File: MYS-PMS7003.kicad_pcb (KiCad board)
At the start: 2 copper layers, 92 x 60 mm, 42 parts, among them P1 CONN_02X04, P2 CONN_01X03, P3 CONN_01X08, P4 CONN_01X04, P5 CONN_01X04, P6 CONN_02X11, P7 CONN_01X06, U1 Arduino_Pro_Micro, U2 M3_Mounting_hole, U3 M3_Mounting_hole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

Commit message: Added text to silkscreen, added Gerber files, schematic.
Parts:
- added G***: LOGO, Open_Hardware:Full_OSHW_scaled, F.Cu at (89.0, 59.5)
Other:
- board text added: "MYS-PMS7003 Rev.0"
- board text added: "https://github.com/dirkjankrijnders/MYS-PMS7003"

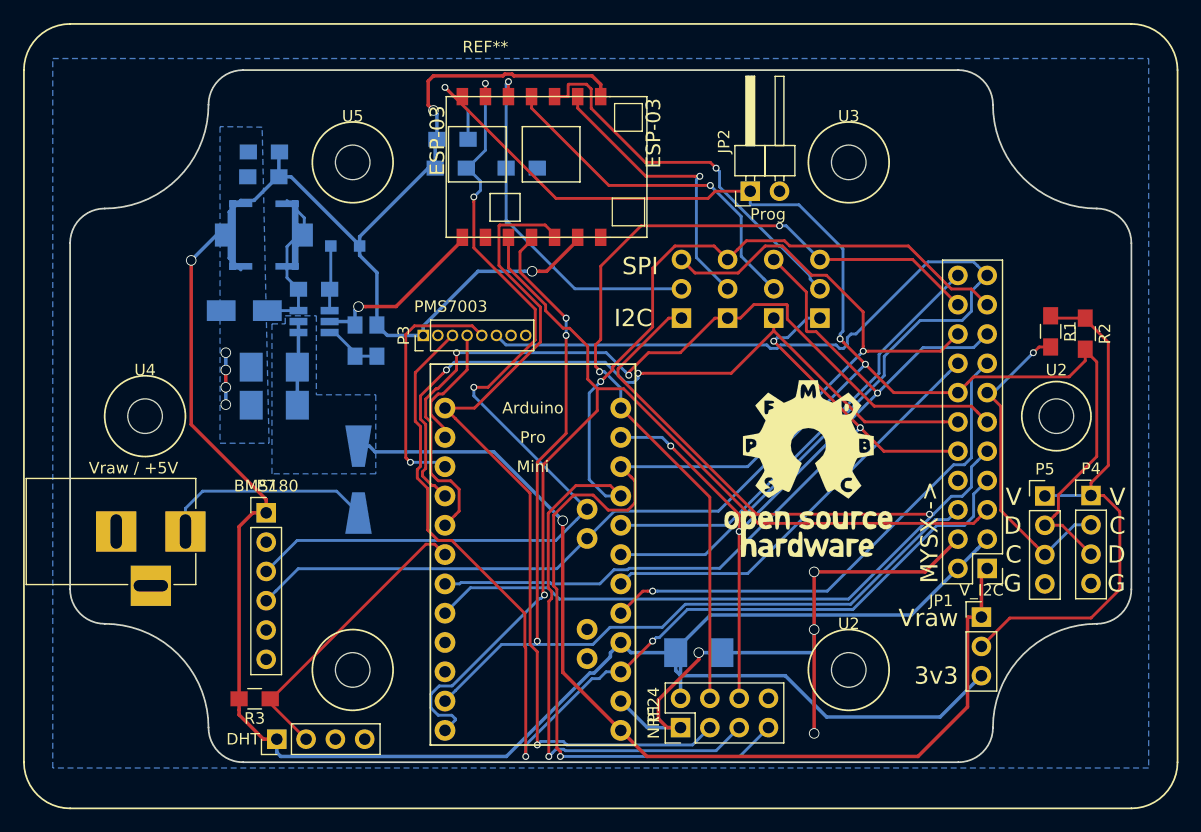
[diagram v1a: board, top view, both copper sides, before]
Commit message: Updated radio module outline, fixed missing tracks
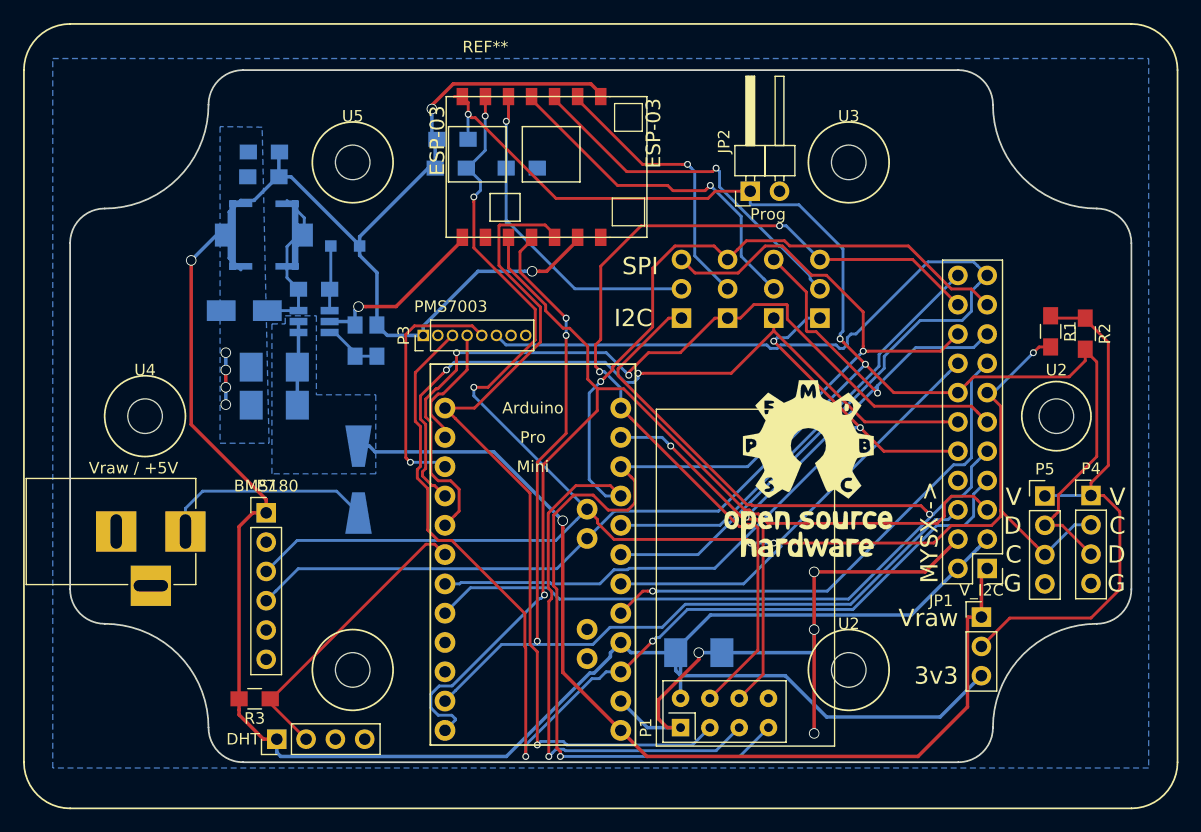
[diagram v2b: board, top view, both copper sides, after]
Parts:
- P1: footprint Pin_Headers:Pin_Header_Straight_2x04_Pitch2.54mm -> RF_Modules:nRF24L01_Breakout
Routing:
- net /MYSX_D7_SCL: track 107.1 -> 143.5 mm, vias 4 -> 6
- net /MYSX_D8_SDA: track 164.9 -> 159.3 mm
- net /MYSX_D14_CS: track 77.4 -> 81.9 mm
- net +3V3: track 245.1 -> 242.2 mm
- net Net-(JP4-Pad2): track 31.4 -> 28.8 mm
- net Net-(JP3-Pad2): track 33.3 -> 31.2 mm
- net /MYSX_D11_MOSI: track 73.3 -> 75.2 mm
- net /MYSX_D1_DFM: track 94.1 -> 95.8 mm
- net Net-(JP5-Pad2): track 25.0 -> 24.3 mm

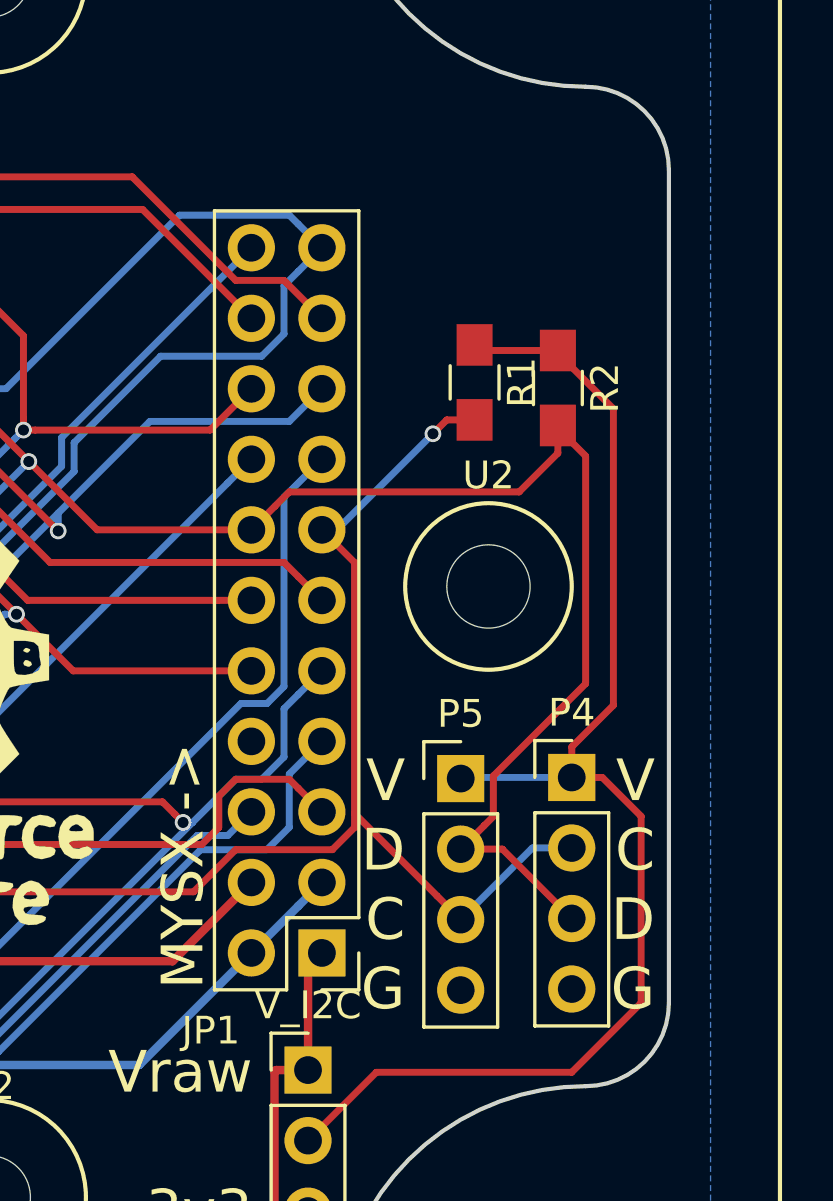
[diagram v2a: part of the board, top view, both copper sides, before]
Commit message: Created a slot for the MYSX cable to go to the other side of the board
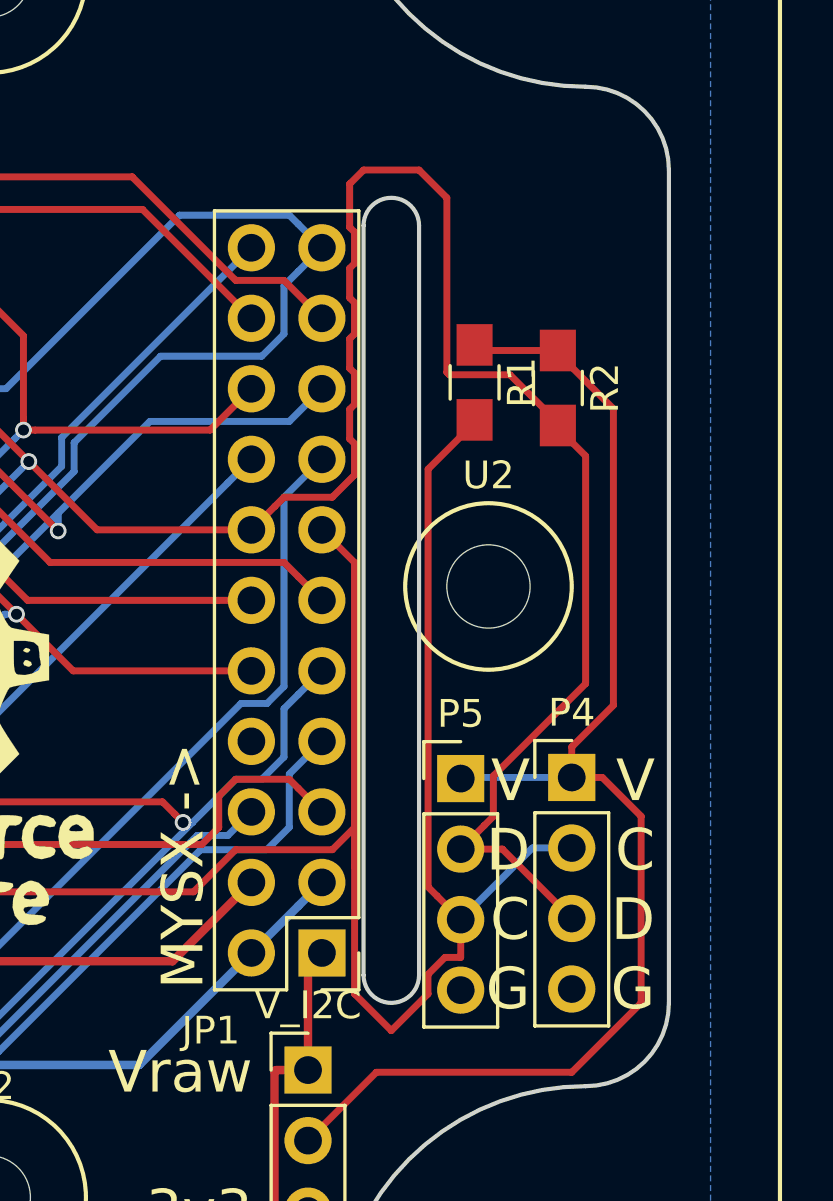
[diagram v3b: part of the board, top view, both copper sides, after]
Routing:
- net /MYSX_D7_SCL: track 143.5 -> 163.9 mm, vias 6 -> 5
- net /MYSX_D8_SDA: track 159.3 -> 176.9 mm
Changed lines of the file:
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@@
     (area 20.721799 20.721799 121.278201 89.278201)
     (thickness 1.6)
-    (drawings 15)
-    (tracks 702)
+    (drawings 19)
+    (tracks 731)
     (zones 0)
     (modules 43)
@@
       (net 22 "Net-(P1-Pad8)"))
   )
+  (gr_line (start 108 69) (end 108 42) (layer Edge.Cuts) (width 0.15))
+  (gr_line (start 106 42) (end 106 69) (layer Edge.Cuts) (width 0.15))
+  (gr_arc (start 107 42) (end 106 42) (angle 180) (layer Edge.Cuts) (width 0.15))
+  (gr_arc (start 107 69) (end 108 69) (angle 180) (layer Edge.Cuts) (width 0.15))
   (gr_text https://github.com/dirkjankrijnders/MYS-PMS7003 (at 62.5 37) (layer B.SilkS)
     (effects (font (size 0.75 0.75) (thickness 0.15)) (justify mirror))
@@
     (effects (font (size 1.5 1.5) (thickness 0.3)) (justify right))
   )
-  (gr_text G (at 107.5 69.5) (layer F.SilkS)
+  (gr_text G (at 112 69.5) (layer F.SilkS)
     (effects (font (size 1.5 1.5) (thickness 0.3)) (justify right))
   )
-  (gr_text C (at 107.5 67) (layer F.SilkS)
+  (gr_text C (at 112 67) (layer F.SilkS)
     (effects (font (size 1.5 1.5) (thickness 0.3)) (justify right))
   )
-  (gr_text D (at 107.5 64.5) (layer F.SilkS)
+  (gr_text D (at 112 64.5) (layer F.SilkS)
     (effects (font (size 1.5 1.5) (thickness 0.3)) (justify right))
   )
-  (gr_text V (at 107.5 62) (layer F.SilkS)
+  (gr_text V (at 112 62) (layer F.SilkS)
     (effects (font (size 1.5 1.5) (thickness 0.3)) (justify right))
   )
@@
   (segment (start 113.5 61.88) (end 109.54 61.88) (width 0.25) (layer B.Cu) (net 7))
   (segment (start 109.54 61.88) (end 109.5 61.92) (width 0.25) (layer B.Cu) (net 7))
+  (segment (start 113 49.2) (end 113 49.1) (width 0.25) (layer F.Cu) (net 8))
+  (segment (start 109.089999 47.375001) (end 109 47.285002) (width 0.25) (layer F.Cu) (net 8))
+  (segment (start 111.275001 47.375001) (end 109.089999 47.375001) (width 0.25) (layer F.Cu) (net 8))
+  (segment (start 113 49.1) (end 111.275001 47.375001) (width 0.25) (layer F.Cu) (net 8))
+  (segment (start 109 41) (end 108 40) (width 0.25) (layer F.Cu) (net 8))
+  (segment (start 109 47.285002) (end 109 41) (width 0.25) (layer F.Cu) (net 8))
+  (segment (start 105.675001 44.775999) (end 105.675001 45.904001) (width 0.25) (layer F.Cu) (net 8))
+  (segment (start 105.5 44.600998) (end 105.675001 44.775999) (width 0.25) (layer F.Cu) (net 8))
+  (segment (start 105.5 43.539002) (end 105.5 44.600998) (width 0.25) (layer F.Cu) (net 8))
+  (segment (start 105.675001 43.364001) (end 105.5 43.539002) (width 0.25) (layer F.Cu) (net 8))
+  (segment (start 105.675001 42.235999) (end 105.675001 43.364001) (width 0.25) (layer F.Cu) (net 8))
+  (segment (start 108 40) (end 106 40) (width 0.25) (layer F.Cu) (net 8))
+  (segment (start 105.5 42.060998) (end 105.675001 42.235999) (width 0.25) (layer F.Cu) (net 8))
+  (segment (start 105.5 40.5) (end 105.5 42.060998) (width 0.25) (layer F.Cu) (net 8))
+  (segment (start 106 40) (end 105.5 40.5) (width 0.25) (layer F.Cu) (net 8))
+  (segment (start 105.675001 45.904001) (end 105.5 46.079002) (width 0.25) (layer F.Cu) (net 8))
+  (segment (start 105.5 46.079002) (end 105.5 47.140998) (width 0.25) (layer F.Cu) (net 8))
+  (segment (start 105.5 47.140998) (end 105.675001 47.315999) (width 0.25) (layer F.Cu) (net 8))
+  (segment (start 105.675001 47.315999) (end 105.675001 48.444001) (width 0.25) (layer F.Cu) (net 8))
+  (segment (start 105.675001 48.444001) (end 105.5 48.619002) (width 0.25) (layer F.Cu) (net 8))
+  (segment (start 105.5 48.619002) (end 105.5 49.680998) (width 0.25) (layer F.Cu) (net 8))
+  (segment (start 105.5 49.680998) (end 105.675001 49.855999) (width 0.25) (layer F.Cu) (net 8))
+  (segment (start 105.675001 49.855999) (end 105.675001 50.984001) (width 0.25) (layer F.Cu) (net 8))
+  (segment (start 105.675001 50.984001) (end 104.874003 51.784999) (width 0.25) (layer F.Cu) (net 8))
+  (segment (start 104.874003 51.784999) (end 103.135001 51.784999) (width 0.25) (layer F.Cu) (net 8))
+  (segment (start 103.135001 51.784999) (end 102.809999 52.110001) (width 0.25) (layer F.Cu) (net 8))
+  (segment (start 102.809999 52.110001) (end 101.96 52.96) (width 0.25) (layer F.Cu) (net 8))
   (segment (start 59.5122 28.829) (end 59.812199 29.128999) (width 0.25) (layer F.Cu) (net 8))
   (segment (start 59.812199 29.128999) (end 60.128999 29.128999) (width 0.25) (layer F.Cu) (net 8))
@@
   (segment (start 44.774999 68.225001) (end 42.849999 70.150001) (width 0.25) (layer B.Cu) (net 8))
   (segment (start 42.849999 70.150001) (end 42 71) (width 0.25) (layer B.Cu) (net 8))
-  (segment (start 113 49.2) (end 113 50.2) (width 0.25) (layer F.Cu) (net 8))
-  (segment (start 113 50.2) (end 111.604999 51.595001) (width 0.25) (layer F.Cu) (net 8))
-  (segment (start 111.604999 51.595001) (end 103.324999 51.595001) (width 0.25) (layer F.Cu) (net 8))
-  (segment (start 103.324999 51.595001) (end 102.809999 52.110001) (width 0.25) (layer F.Cu) (net 8))
-  (segment (start 102.809999 52.110001) (end 101.96 52.96) (width 0.25) (layer F.Cu) (net 8))
   (segment (start 109.5 64.46) (end 111 64.46) (width 0.25) (layer F.Cu) (net 8))
   (segment (start 111 64.46) (end 113.5 66.96) (width 0.25) (layer F.Cu) (net 8))
@@
   (segment (start 92.374998 48.199998) (end 92.699998 47.874998) (width 0.25) (layer B.Cu) (net 28))
   (segment (start 86.300001 49.125001) (end 86.600001 48.825001) (width 0.25) (layer B.Cu) (net 28))
+  (segment (start 110 49) (end 110 49.1) (width 0.25) (layer F.Cu) (net 31))
+  (segment (start 110 49.1) (end 108.324999 50.775001) (width 0.25) (layer F.Cu) (net 31))
+  (segment (start 108.324999 50.775001) (end 108.324999 65.824999) (width 0.25) (layer F.Cu) (net 31))
+  (segment (start 108.324999 65.824999) (end 108.650001 66.150001) (width 0.25) (layer F.Cu) (net 31))
+  (segment (start 108.650001 66.150001) (end 109.5 67) (width 0.25) (layer F.Cu) (net 31))
+  (segment (start 105.675001 63.175001) (end 105.675001 65.091263) (width 0.25) (layer F.Cu) (net 31))
+  (segment (start 105.678201 65.094463) (end 105.678201 69.678201) (width 0.25) (layer F.Cu) (net 31))
+  (segment (start 105.675001 65.091263) (end 105.678201 65.094463) (width 0.25) (layer F.Cu) (net 31))
+  (segment (start 105.678201 69.678201) (end 107 71) (width 0.25) (layer F.Cu) (net 31))
+  (segment (start 107 71) (end 108.321799 69.678201) (width 0.25) (layer F.Cu) (net 31))
+  (segment (start 108.321799 69.678201) (end 108.321799 68.974463) (width 0.25) (layer F.Cu) (net 31))
+  (segment (start 108.321799 68.974463) (end 108.934463 68.361799) (width 0.25) (layer F.Cu) (net 31))
+  (segment (start 108.934463 68.361799) (end 109.5 68.361799) (width 0.25) (layer F.Cu) (net 31))
+  (segment (start 109.5 68.361799) (end 109.5 67) (width 0.25) (layer F.Cu) (net 31))
   (segment (start 86 66) (end 99.876262 66) (width 0.25) (layer F.Cu) (net 31))
   (segment (start 99.876262 66) (end 101.394463 64.481799) (width 0.25) (layer F.Cu) (net 31))
@@
   (segment (start 67.107001 65.774999) (end 68.919001 63.962999) (width 0.25) (layer B.Cu) (net 31))
   (segment (start 42 68.46) (end 44.685001 65.774999) (width 0.25) (layer B.Cu) (net 31))
-  (segment (start 108.5 49.5) (end 105.04 52.96) (width 0.25) (layer B.Cu) (net 31))
-  (segment (start 105.04 52.96) (end 104.5 52.96) (width 0.25) (layer B.Cu) (net 31))
-  (segment (start 110 49) (end 109 49) (width 0.25) (layer F.Cu) (net 31))
-  (segment (start 109 49) (end 108.5 49.5) (width 0.25) (layer F.Cu) (net 31))
-  (via (at 108.5 49.5) (size 0.6) (drill 0.4) (layers F.Cu B.Cu) (net 31))
   (segment (start 104.5 52.96) (end 105.675001 54.135001) (width 0.25) (layer F.Cu) (net 31))
   (segment (start 105.675001 54.135001) (end 105.675001 63.175001) (width 0.25) (layer F.Cu) (net 31))
-  (segment (start 105.675001 63.175001) (end 108.650001 66.150001) (width 0.25) (layer F.Cu) (net 31))
-  (segment (start 108.650001 66.150001) (end 109.5 67) (width 0.25) (layer F.Cu) (net 31))
   (segment (start 113.5 64.42) (end 112.08 64.42) (width 0.25) (layer B.Cu) (net 31))
   (segment (start 112.08 64.42) (end 109.5 67) (width 0.25) (layer B.Cu) (net 31))

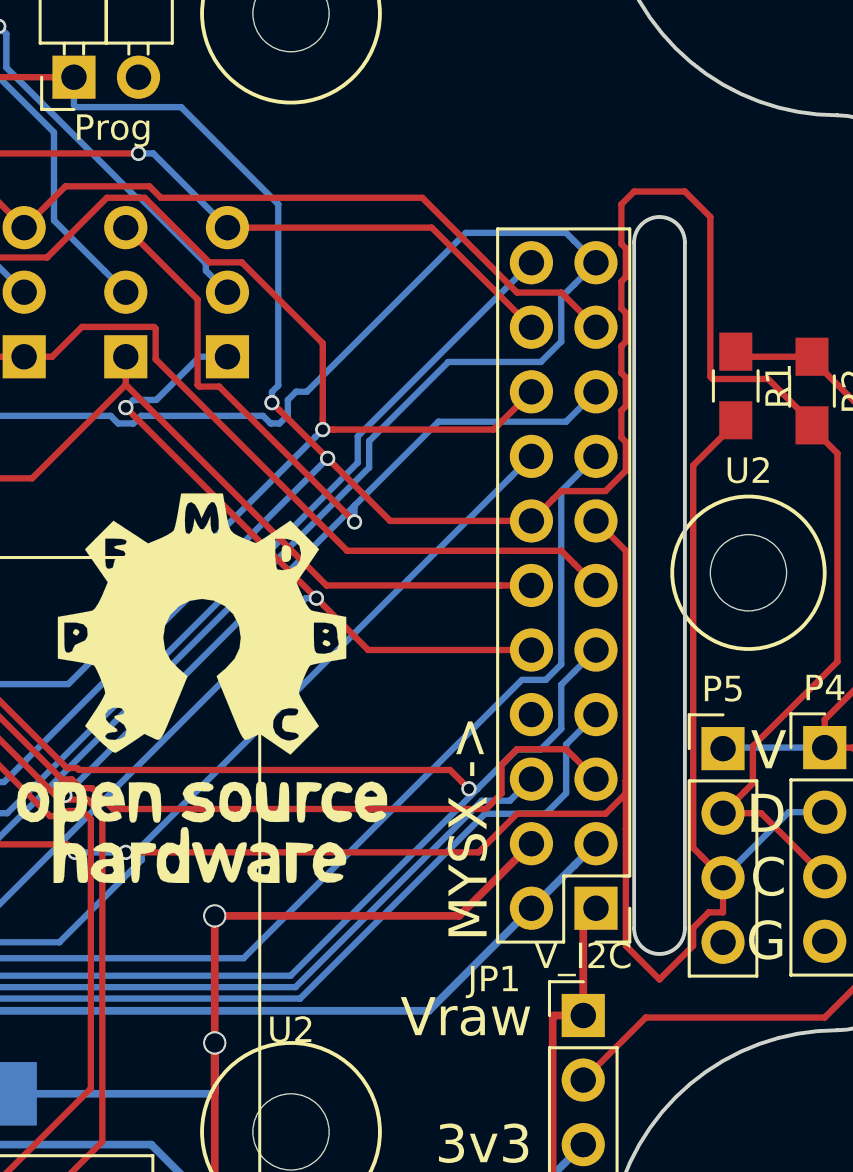
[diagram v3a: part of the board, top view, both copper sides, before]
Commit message: Switched from the standard footprint to the official MYSX 2.6 footprint
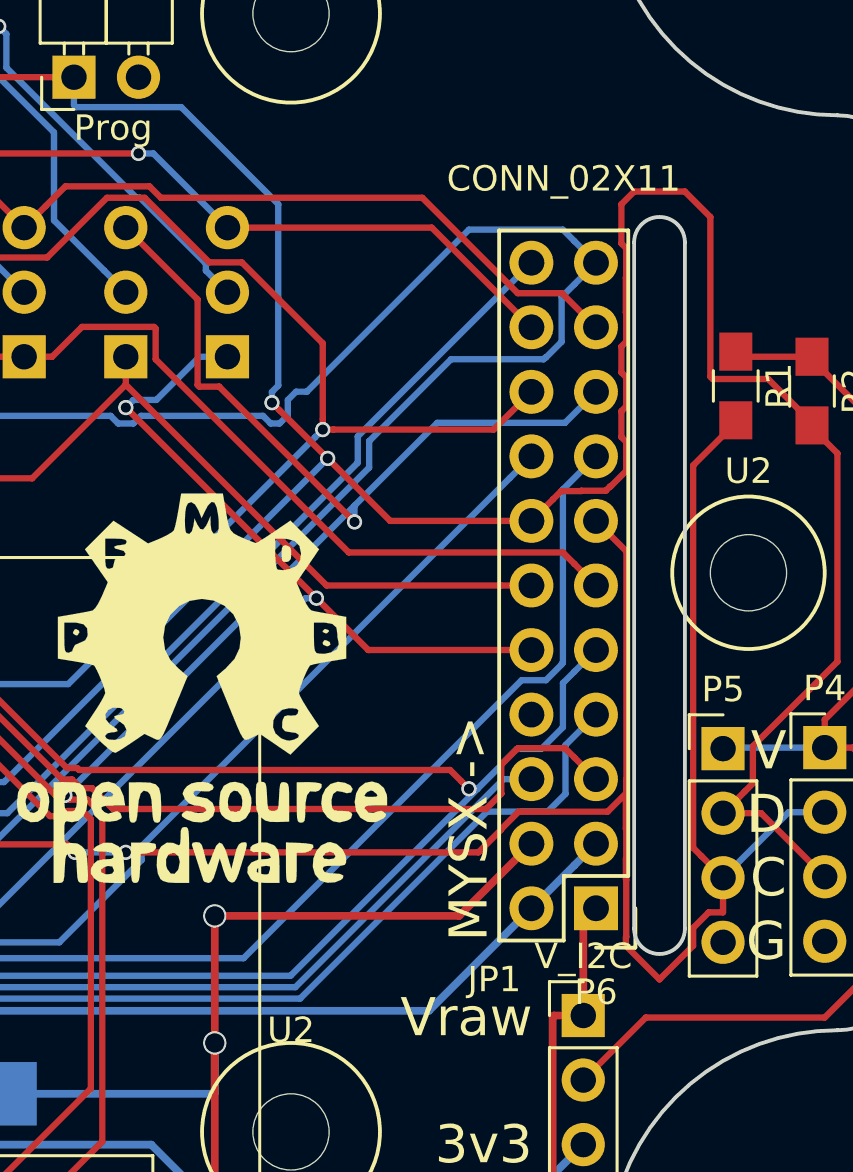
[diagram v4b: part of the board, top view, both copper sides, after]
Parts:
- P6: footprint Pin_Headers:Pin_Header_Straight_2x11_Pitch2.54mm -> mysensors_connectors:MYSX_2.6
